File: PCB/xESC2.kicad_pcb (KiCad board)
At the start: 4 copper layers, 49.5 x 29 mm, 108 parts, among them J1 Conn_01x06_Male, J10 Conn_01x06_Male, J2 USB_B_Micro, J3 Conn_01x05_Male, J4 Conn_01x05_Male, J5 Conn_01x03_Male, J6 Conn_02x02_Counter_Clockwise, J7 Conn_02x02_Counter_Clockwise, J8 Conn_02x02_Counter_Clockwise, J9 Conn_01x06_Male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

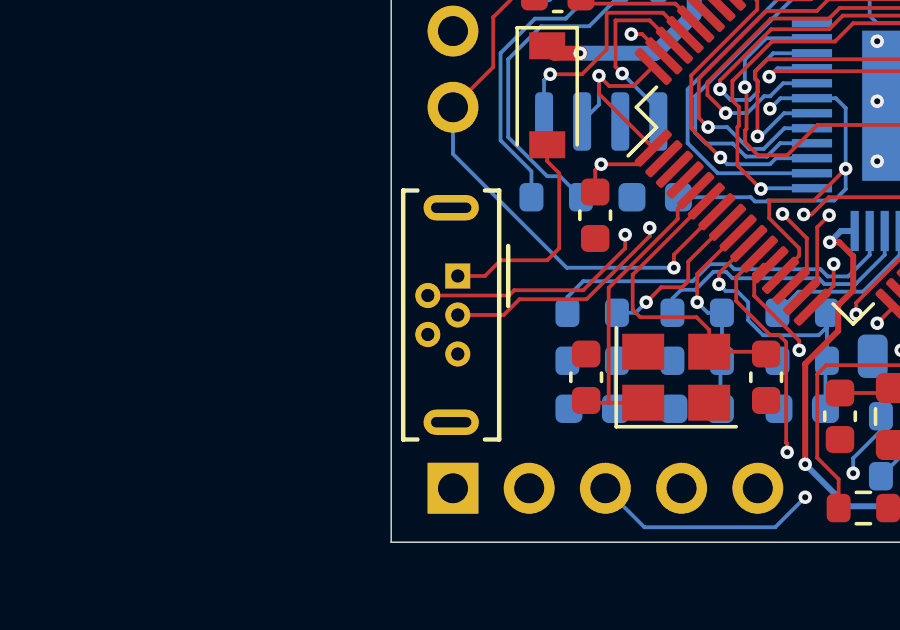
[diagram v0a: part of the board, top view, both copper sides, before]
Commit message: Updated Y1 Part Number
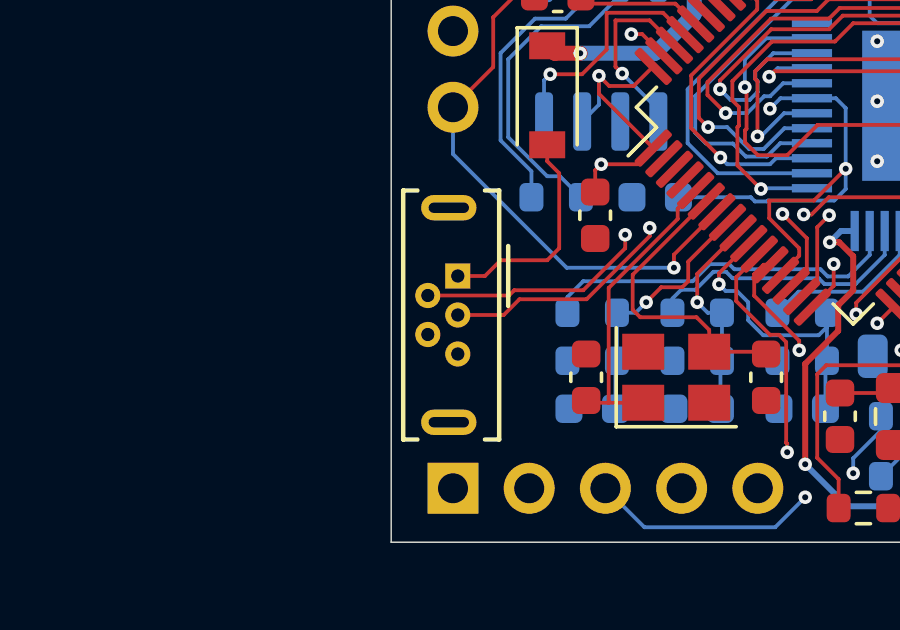
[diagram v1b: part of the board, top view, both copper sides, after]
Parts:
- J2: footprint Connector_USB:USB_Micro-B_Wuerth_614105150721_Vertical -> xESC2:USB_Micro
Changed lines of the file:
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@@
 			)
 		)
-		(property "LCSC" "C49217"
+		(property "LCSC" "C377773"
 			(at 0 0 0)
 			(layer "F.Fab")
@@
 			)
 		)
-		(property "JLC" "C49217"
+		(property "JLC" "C377773"
 			(at 0 0 -90)
 			(unlocked yes)
@@
 			)
 		)
-		(property "LCSC" "C49217"
+		(property "LCSC" "C377773"
 			(at 0 0 0)
 			(layer "F.Fab")
@@
 			)
 		)
-		(property "JLC" "C49217"
+		(property "JLC" "C377773"
 			(at 0 0 90)
 			(unlocked yes)
@@
 			)
 		)
-		(property "LCSC" "C49217"
+		(property "LCSC" "C377773"
 			(at 0 0 0)
 			(layer "F.Fab")
@@
 			)
 		)
-		(property "JLC" "C49217"
+		(property "JLC" "C377773"
 			(at 0 0 90)
 			(unlocked yes)
@@
 			)
 		)
-		(property "LCSC" "C2442665"
+		(property "LCSC" "C2682775"
 			(at 0 0 0)
 			(layer "F.Fab")
@@
 			)
 		)
-		(property "JLC" "C2442665"
+		(property "JLC" "C2682775"
 			(at 0 0 0)
 			(unlocked yes)
@@
 			)
 		)
-		(property "LCSC" "C49217"
+		(property "LCSC" "C377773"
 			(at 0 0 0)
 			(layer "F.Fab")
@@
 			)
 		)
-		(property "JLC" "C49217"
+		(property "JLC" "C377773"
 			(at 0 0 0)
 			(unlocked yes)
@@
 		)
 	)
-	(footprint "Connector_USB:USB_Micro-B_Wuerth_614105150721_Vertical"
+	(footprint "xESC2:USB_Micro"
 		(layer "F.Cu")
 		(at 231.22 124.025 -90)
@@
 			)
 		)
-		(property "Footprint" "Connector_USB:USB_Micro-B_Wuerth_614105150721_Vertical"
+		(property "Footprint" "xESC2:USB_Micro"
 			(at 0 0 -90)
 			(unlocked yes)
@@
 			)
 		)
-		(property "JLC" "C668588"
+		(property "JLC" "C145795"
 			(at 0 0 -90)
 			(unlocked yes)
@@
 		)
 		(pad "6" thru_hole oval
-			(at -2.275 0.22 270)
+			(at -2.275 0.3 270)
 			(size 0.85 1.85)
 			(drill oval 0.35 1.35)
@@
 		)
 		(pad "6" thru_hole oval
-			(at 4.875 0.22 270)
+			(at 4.875 0.3 270)
 			(size 0.85 1.85)
 			(drill oval 0.35 1.35)
@@
 			(pintype "passive")
 		)
-		(model "${KIPRJMOD}/libs/MicroUSB.step"
+		(model "${KICAD8_3DMODEL_DIR}/Connector_USB.3dshapes/USB_Micro-B_Wuerth_614105150721_Vertical.wrl"
 			(offset
-				(xyz 4.2 -2.9 -1.5)
+				(xyz 0 0 0)
 			)
 			(scale
@@
 			)
 		)
-		(property "LCSC" "C49217"
+		(property "LCSC" "C377773"
 			(at 0 0 0)
 			(layer "B.Fab")
@@
 			)
 		)
-		(property "JLC" "C49217"
+		(property "JLC" "C377773"
 			(at 0 0 0)
 			(unlocked yes)
@@
 			)
 		)
-		(property "LCSC" "C49217"
+		(property "LCSC" "C377773"
 			(at 0 0 0)
 			(layer "B.Fab")
@@
 			)
 		)
-		(property "JLC" "C49217"
+		(property "JLC" "C377773"
 			(at 0 0 180)
 			(unlocked yes)
@@
 			)
 		)
-		(property "LCSC" "C2985721"
+		(property "LCSC" "C2903495"
 			(at 0 0 0)
 			(layer "B.Fab")
@@
 			)
 		)
-		(property "JLC" "C2985721"
+		(property "JLC" "C2903495"
 			(at 0 0 180)
 			(unlocked yes)
@@
 			)
 		)
-		(property "LCSC" "C2985721"
+		(property "LCSC" "C2903495"
 			(at 0 0 0)
 			(layer "B.Fab")
@@
 			)
 		)
-		(property "JLC" "C2985721"
+		(property "JLC" "C2903495"
 			(at 0 0 180)
 			(unlocked yes)
@@
 			)
 		)
-		(property "LCSC" "C2985721"
+		(property "LCSC" "C2903495"
 			(at 0 0 0)
 			(layer "B.Fab")
@@
 			)
 		)
-		(property "JLC" "C2985721"
+		(property "JLC" "C2903495"
 			(at 0 0 180)
 			(unlocked yes)
@@
 		(polygon
 			(pts
-				(xy 278.5 144) (xy 195.25 142.625) (xy 194.75 97.375) (xy 279.5 98.25)
+				(xy 279.85 144.125) (xy 195.25 142.625) (xy 194.75 97.375) (xy 279.5 98.25)
 			)
 		)
@@
 		(polygon
 			(pts
-				(xy 277.75 142) (xy 252.7875 141.6875) (xy 252.8125 98.7125) (xy 279.25 99.5)
+				(xy 279.625 142.075) (xy 252.7875 141.6875) (xy 252.8125 98.7125) (xy 279.25 99.5)
 			)
 		)
